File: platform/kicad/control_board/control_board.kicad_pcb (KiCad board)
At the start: 2 copper layers, 81.5 x 131.5 mm, 71 parts, among them J1 DHT22, J10 ADC1,7, J11 Qwiic JST, J12 Data 1, J13 Data 2, J14 ROUTER 24V, J15 24V/5V OUT, J16 Data 3, J17 PoE 2, J18 Conn_01x03, J19 Conn_01x03, J2 DS18B20, J3 Conn_01x04, J4 24V IN, J5 Conn_01x05_Pin, J6 PoE 1, J7 PoE 3, J8 UART, J9 ADC1,6, K1 LCA717, K2 LCA717, K3 LCA717, K4 LCA717, U1 ESP32-DevKitC, U2 ACS722xLCTR-20AU, U3 AP63205WU-7, U4 AP63205WU-7

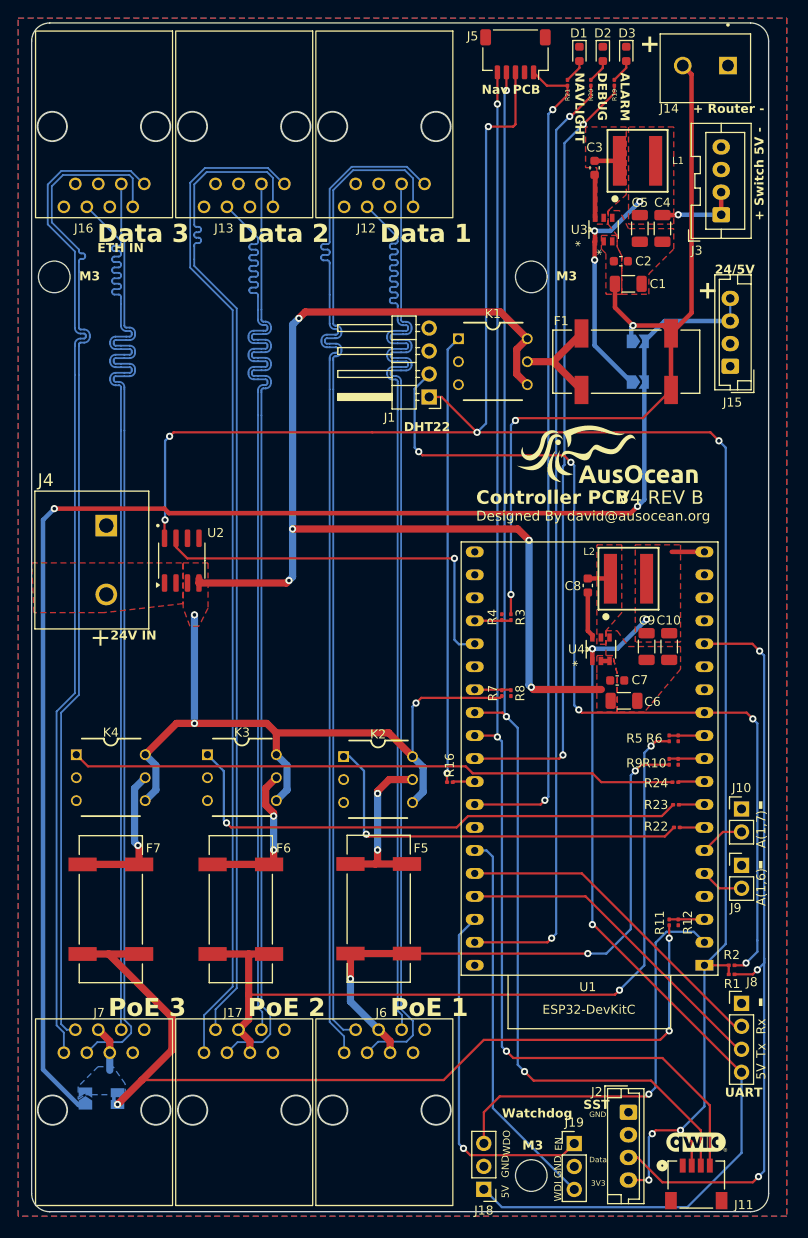
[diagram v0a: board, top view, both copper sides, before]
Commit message: Controller PCB: Update connector positions (#21)
This change slightly alters the positioning of some connectors to increase the usability of the board.
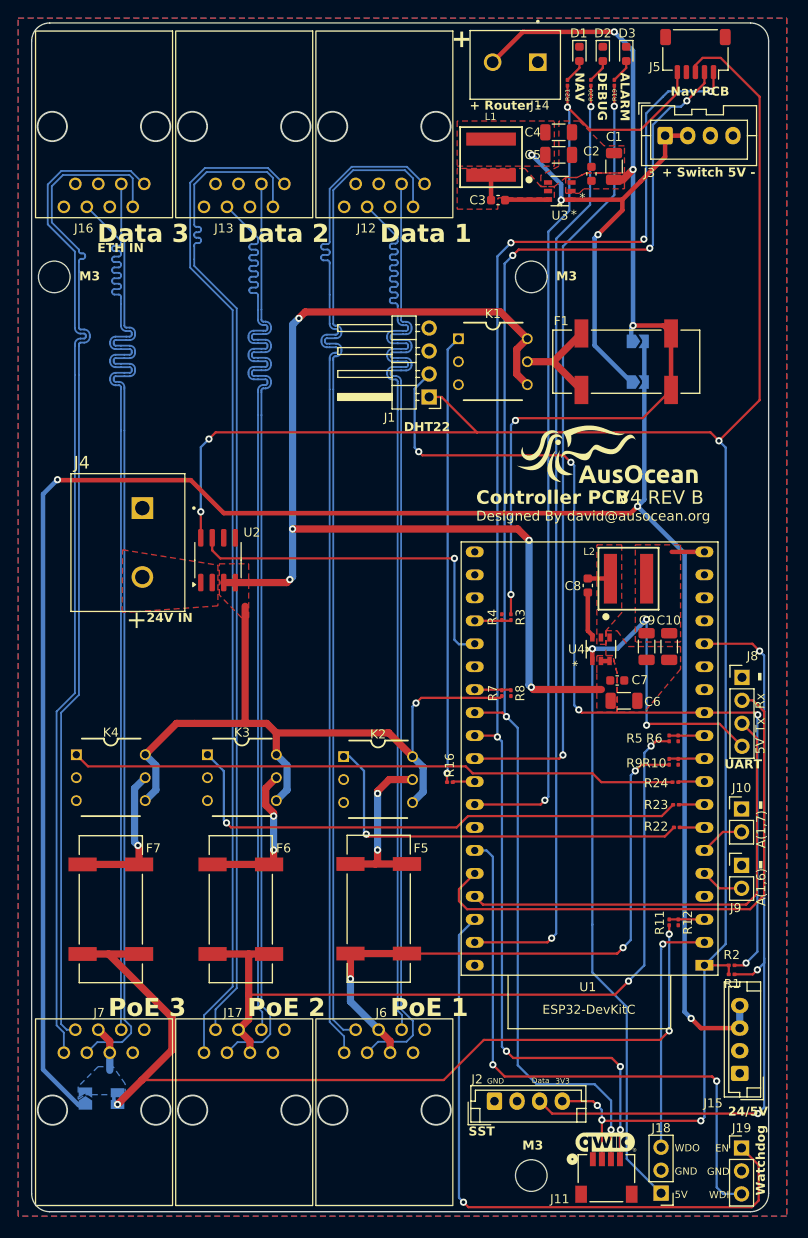
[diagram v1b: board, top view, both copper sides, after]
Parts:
- moved J15 78.2 mm to (164.0, 141.4)
- moved J8 36.1 mm to (164.2, 97.6)
- moved J14 21.0 mm to (141.7, 29.5)
- moved J5 19.9 mm to (159.1, 28.6)
- moved J18 19.6 mm to (155.3, 154.6)
- moved J19 18.5 mm to (164.2, 149.6)
- moved L1 16.2 mm to (136.5, 40.1), turned to 180 degrees
- moved C4 15.6 mm to (144.0, 37.3), turned to 0 degrees
- moved J2 14.9 mm to (136.9, 144.4), turned to 0 degrees
- moved C1 13.1 mm to (150.1, 41.1), turned to 90 degrees
- moved C5 12.1 mm to (144.0, 39.8), turned to 0 degrees
- moved C3 11.3 mm to (137.3, 44.8), turned to 180 degrees
- moved J3 10.7 mm to (155.7, 37.7), turned to 0 degrees
- moved C2 10.2 mm to (147.6, 41.9), turned to 90 degrees
- moved G*** 10.0 mm to (149.1, 148.9)
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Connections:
- J5 pad 1: Navlight -> SCL
- J5 pad 2: GND -> SDA
- J5 pad 4: SDA -> GND
- J5 pad 5: SCL -> Navlight
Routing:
- net 5-24VOUT: track 165.4 -> 224.2 mm, vias 2 -> 3
- net WD_EN*: track 39.4 -> 72.0 mm
- net RX: track 36.5 -> 61.8 mm
- net WD_IN: track 42.8 -> 65.6 mm, vias 0 -> 2
- net EN: track 46.0 -> 27.4 mm
- net TX: track 36.5 -> 51.6 mm
- net NW_out: track 89.3 -> 103.6 mm, vias 3 -> 5
- net NW_5V: track 33.8 -> 47.8 mm, vias 4 -> 3
- net Navlight: track 92.4 -> 105.4 mm
- net SCL: track 142.9 -> 155.9 mm, vias 3 -> 7
- net SDA: track 141.3 -> 150.7 mm, vias 3 -> 5
- net 5VIN: track 106.8 -> 99.0 mm
- net +3V3: track 220.5 -> 226.8 mm, vias 8 -> 6
- net I_in: track 43.8 -> 40.0 mm
- net 24VIN: track 205.7 -> 203.4 mm, vias 8 -> 6
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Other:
- board text added: "NAV"
- board text removed: "NAVLIGHT"
